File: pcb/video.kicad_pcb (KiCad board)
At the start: 4 copper layers, 159.9 x 99.9 mm, 177 parts, among them J1 09031966921, J3 Conn_01x06, J4 Conn_01x06, J5 Conn_01x06, J6 Conn_01x06, J7 DB15_Female_HighDensity, J8 HDMI_A, U1 NCP115, U10 NCA9306DPH, U2 LP3853ESX-3.3/NOPB, U3 LCMXO2-1200HC-4TG100I, U4 LCMXO2-7000HC-4TG144C, U5 THS8136, U6 TFP410PAP, U7 ESD224DQA, U8 ESD224DQA, U9 PCA9540BDP, X1 ASV-xxxMHz

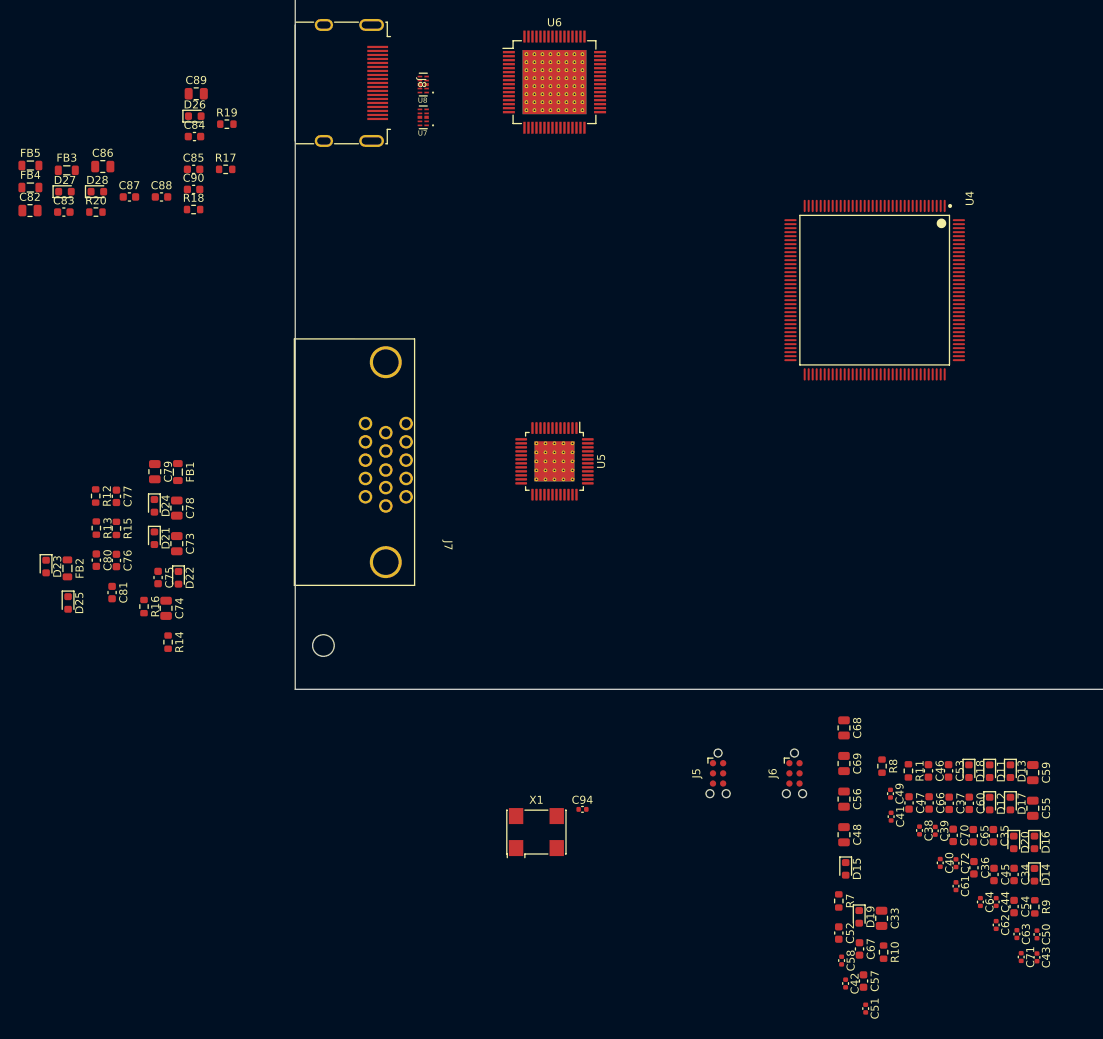
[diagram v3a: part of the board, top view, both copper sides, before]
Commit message: place bypass caps
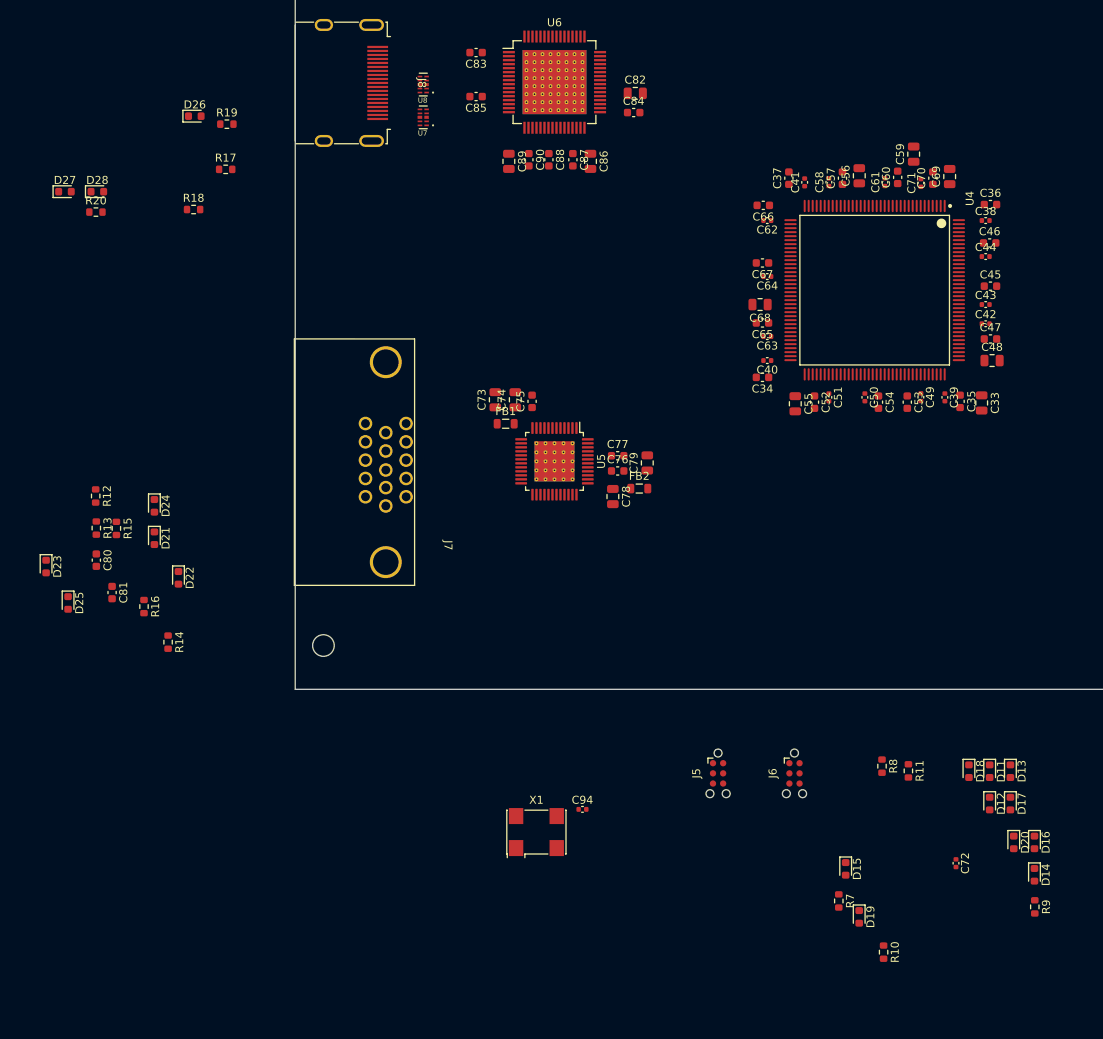
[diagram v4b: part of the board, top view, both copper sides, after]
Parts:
- removed FB3, FB4, FB5: FerriteBead_Small, Inductor_SMD:L_0805_2012Metric
- moved C57 100.4 mm to (123.5, 81.0), turned to 90 degrees
- moved C71 97.6 mm to (133.3, 81.6), turned to 90 degrees
- moved C58 97.3 mm to (121.8, 81.5), turned to 90 degrees
- moved C62 92.6 mm to (114.1, 86.3), turned to 180 degrees
- moved C61 88.4 mm to (128.8, 81.5), turned to 90 degrees
- moved C67 86.6 mm to (113.5, 91.6), turned to 180 degrees
- moved C42 84.3 mm to (141.4, 99.2), turned to 0 degrees
- moved C36 82.9 mm to (142.0, 84.3), turned to 0 degrees
- moved C64 82.6 mm to (114.1, 93.3), turned to 180 degrees
- moved C70 82.2 mm to (134.8, 81.0), turned to 90 degrees
- moved C43 81.9 mm to (141.4, 96.8), turned to 0 degrees
- moved C63 80.9 mm to (114.1, 100.8), turned to 180 degrees
- moved C44 80.7 mm to (141.4, 90.8), turned to 0 degrees
- moved C37 80.7 mm to (116.8, 81.0), turned to 90 degrees
- moved C41 80.0 mm to (118.8, 81.6), turned to 90 degrees
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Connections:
- C82 pad 1: Net-(U6B-DVDD1) -> +3V3
- C83 pad 1: Net-(U6B-DVDD1) -> +3V3
- C84 pad 1: Net-(U6B-DVDD1) -> +3V3
- C85 pad 1: Net-(U6B-DVDD1) -> +3V3
- C86 pad 1: Net-(U6B-TVDD1) -> +3V3
- C87 pad 1: Net-(U6B-TVDD1) -> +3V3
- C88 pad 1: Net-(U6B-TVDD1) -> +3V3
- C89 pad 1: Net-(U6B-PVDD) -> +3V3
- C90 pad 1: Net-(U6B-PVDD) -> +3V3
- U6 pad 1: Net-(U6B-DVDD1) -> +3V3
- U6 pad 12: Net-(U6B-DVDD1) -> +3V3
- U6 pad 18: Net-(U6B-PVDD) -> +3V3
- U6 pad 23: Net-(U6B-TVDD1) -> +3V3
- U6 pad 29: Net-(U6B-TVDD1) -> +3V3
- U6 pad 33: Net-(U6B-DVDD1) -> +3V3

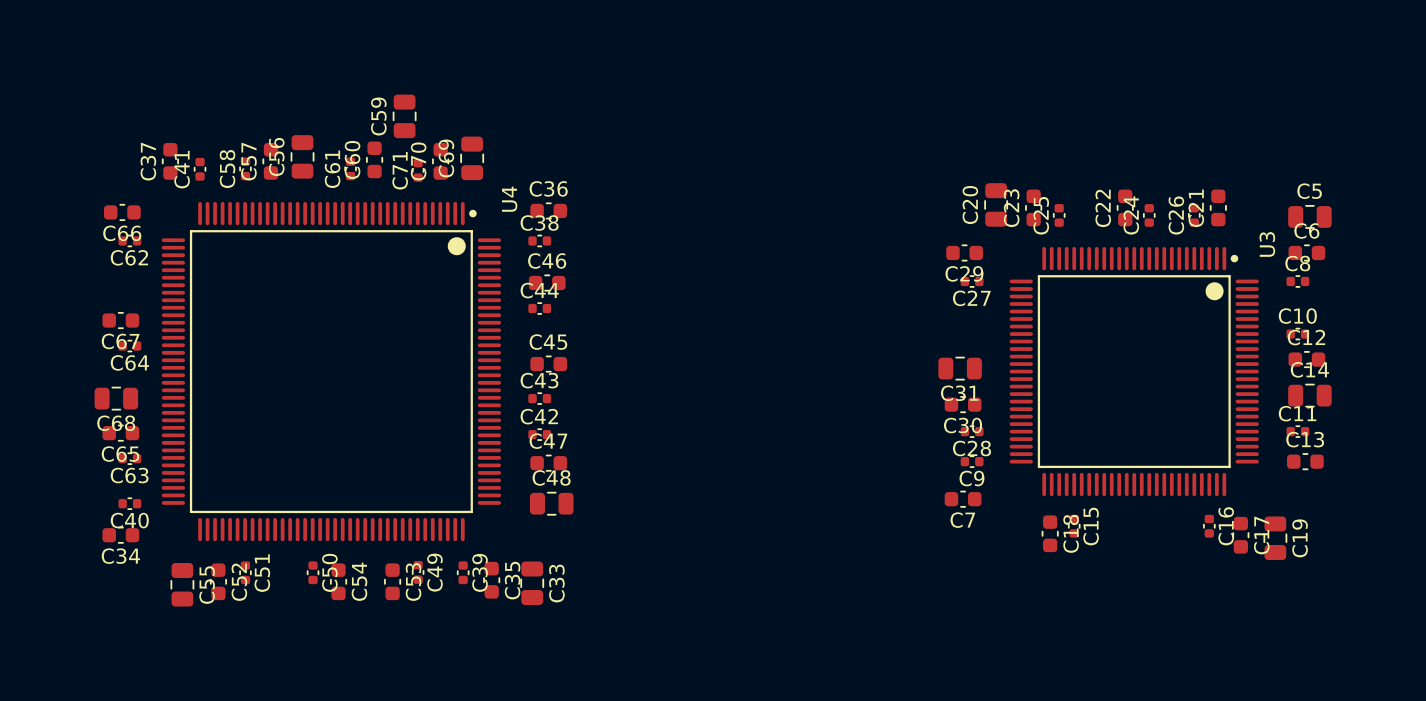
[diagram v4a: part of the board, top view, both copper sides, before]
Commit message: move bypass caps on the bottom
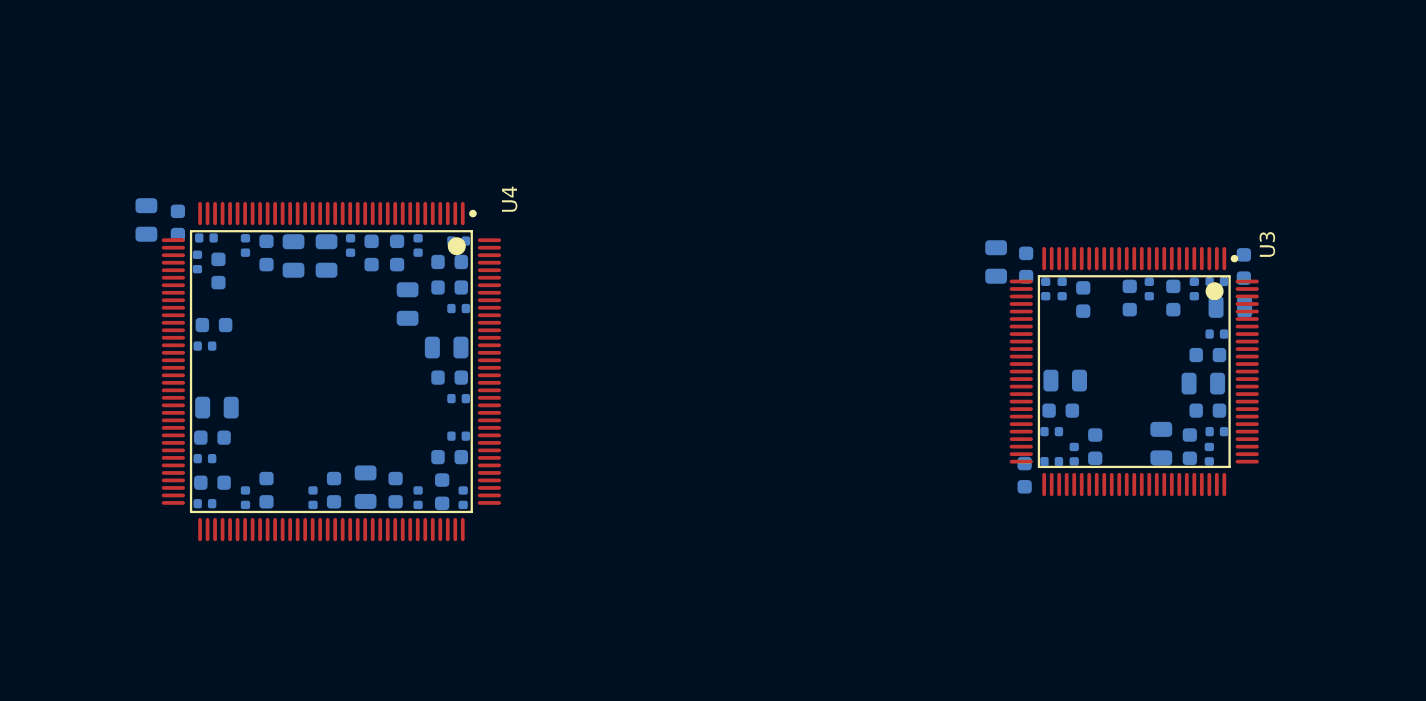
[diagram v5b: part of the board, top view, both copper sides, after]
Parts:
- C10, C11, C12, C13, C14, C15, C16, C17, C18, C19, C20, C21, C22, C23, C24, C25, C26, C27, C28, C29, C30, C31, C33, C34, C35, C36, C37, C38, C39, C40, C41, C42, C43, C44, C45, C46, C47, C48, C49, C5, C50, C51, C52, C53, C54, C55, C56, C57, C58, C59, C6, C60, C61, C62, C63, C64, C65, C66, C67, C68, C69, C7, C70, C71, C8, C9: moved to B.Cu
- moved C33 35.3 mm to (115.2, 84.9), turned to 90 degrees
- moved C55 13.8 mm to (129.8, 102.7), turned to 90 degrees
- moved C48 12.5 mm to (135.2, 93.4), turned to 180 degrees
- moved C59 10.7 mm to (127.2, 87.3), turned to -90 degrees
- moved C69 10.6 mm to (132.6, 90.5), turned to -90 degrees
- moved C19 9.87 mm to (182.8, 99.8), turned to 90 degrees
- moved C5 8.01 mm to (187.4, 90.7), turned to 180 degrees
- moved C66 7.49 mm to (120.0, 88.3), turned to -90 degrees
- moved C36 7.42 mm to (135.4, 87.7), turned to 180 degrees
- moved C13 7.34 mm to (185.9, 97.6), turned to 180 degrees
- moved C14 7.14 mm to (185.6, 95.8)
- moved C31 7.05 mm to (176.4, 95.6), turned to 0 degrees
- moved C34 7.03 mm to (119.6, 102.4), turned to 0 degrees
- moved C23 6.94 mm to (177.6, 90.2), turned to -90 degrees
- moved C52 6.89 mm to (123.2, 102.9), turned to 90 degrees
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
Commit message: place components around connectors
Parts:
- moved R10 86.1 mm to (141.9, 92.7), turned to 0 degrees
- moved X1 77.1 mm to (150.7, 122.1)
- moved C91 76.2 mm to (86.1, 98.8)
- moved C32 74.9 mm to (194.4, 93.6)
- moved C72 74.2 mm to (144.3, 92.7), turned to 90 degrees
- moved R26 73.9 mm to (83.4, 98.8), turned to 90 degrees
- moved R21 72.9 mm to (90.5, 97.0), turned to 180 degrees
- moved U9 72.5 mm to (81.0, 93.3), turned to 90 degrees
- moved U10 72.2 mm to (86.4, 93.3), turned to 90 degrees
- moved R5 71.5 mm to (192.1, 93.5), turned to 0 degrees
- moved R22 71.4 mm to (90.5, 99.0), turned to 180 degrees
- moved C93 70.1 mm to (81.3, 98.8)
- moved C94 69.7 mm to (152.1, 126.4)
- moved R25 65.6 mm to (82.0, 88.0)
- moved R27 65.5 mm to (78.6, 88.0)
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
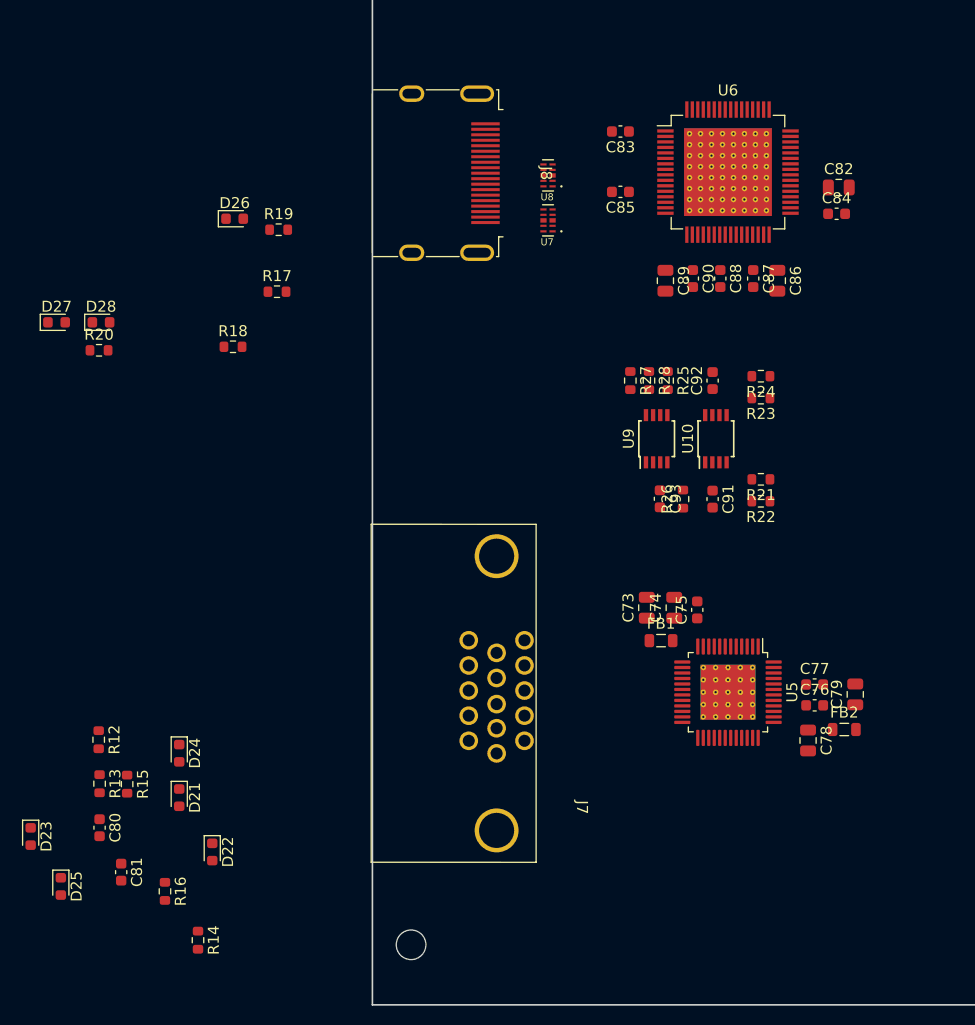
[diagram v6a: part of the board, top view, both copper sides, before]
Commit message: placed all components
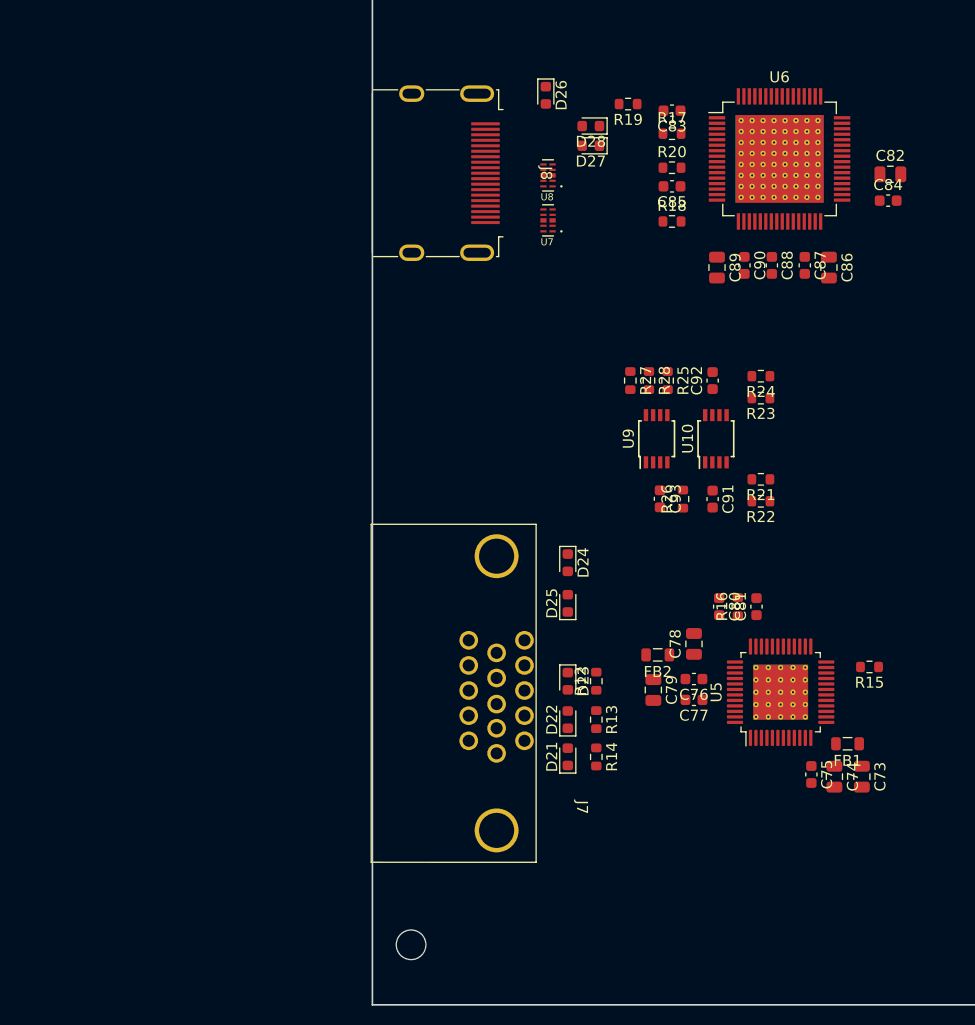
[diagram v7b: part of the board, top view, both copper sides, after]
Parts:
- moved R15 68.5 mm to (100.4, 114.1), turned to 180 degrees
- moved C81 62.8 mm to (90.1, 108.6), turned to 90 degrees
- moved C80 60.0 mm to (86.7, 108.6)
- moved R16 58.3 mm to (88.4, 108.6), turned to 90 degrees
- moved R20 54.8 mm to (82.4, 68.6)
- moved D25 52.9 mm to (72.9, 108.3), turned to 90 degrees
- moved D27 51.3 mm to (75.0, 66.6), turned to 180 degrees
- moved D23 51.0 mm to (72.9, 115.4)
- moved D28 48.1 mm to (75.0, 64.8), turned to 180 degrees
- moved R12 45.7 mm to (75.5, 115.4), turned to 90 degrees
- moved R13 45.6 mm to (75.5, 118.9)
- moved R18 41.6 mm to (82.4, 73.5)
- moved R14 40.0 mm to (75.5, 122.3)
- moved D24 39.4 mm to (72.9, 104.6)
- moved R17 38.8 mm to (82.4, 65.5)
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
